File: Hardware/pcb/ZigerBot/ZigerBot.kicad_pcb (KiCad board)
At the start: 2 copper layers, 107 parts, among them J1 Motor A, J2 M Power, J3 Motor B, J4 4 Pin Male SR-04 Header, J5 USB_B_Micro, J6 3 Pin Male Servo Header, J7 3 Pin Male Servo Header, J8 3 Pin Male Servo Header, J9 3 Pin Male Servo Header, Q1 SMD-MOSFET-P-CH-20V-2A-FDN340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, SW1 SMD Button, SW2 SMD Button, SW3 SMD Button, SW4 SMD Button, U1 L7805CDT-TR, U2 DRV8833PW, U3 ATmega2560-16AU, U4 CP2102N-A01-GQFN24, Y1 16MHz Resonator

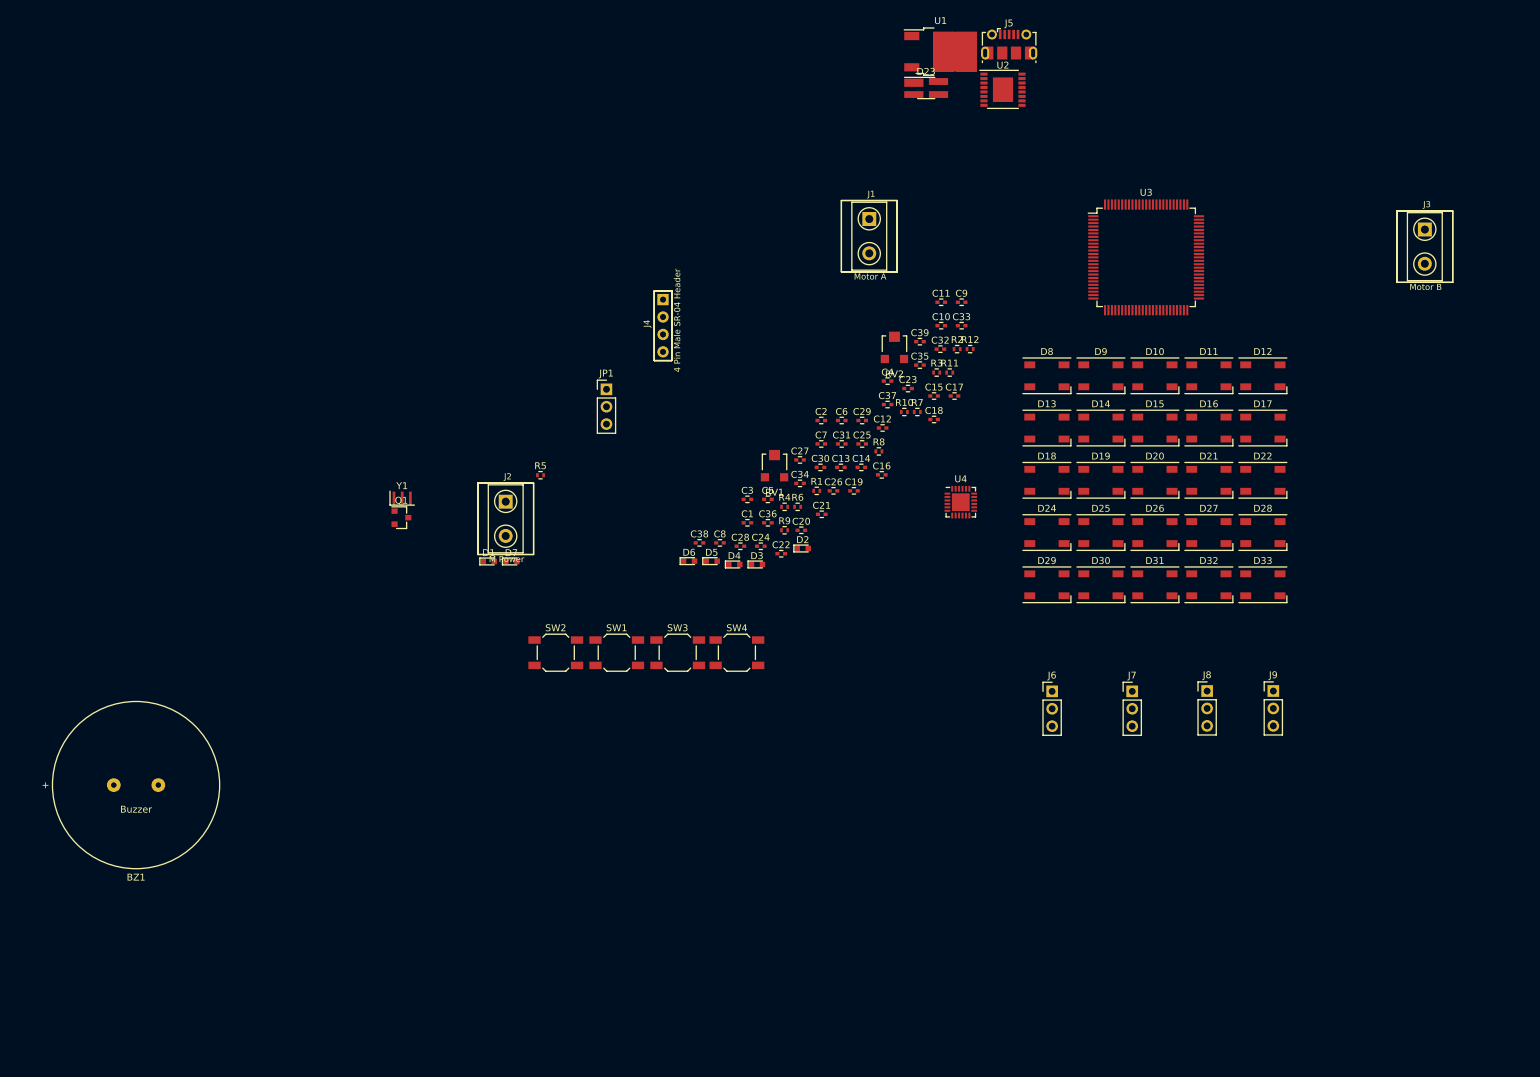
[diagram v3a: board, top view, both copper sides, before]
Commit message: LED-Matrix routed
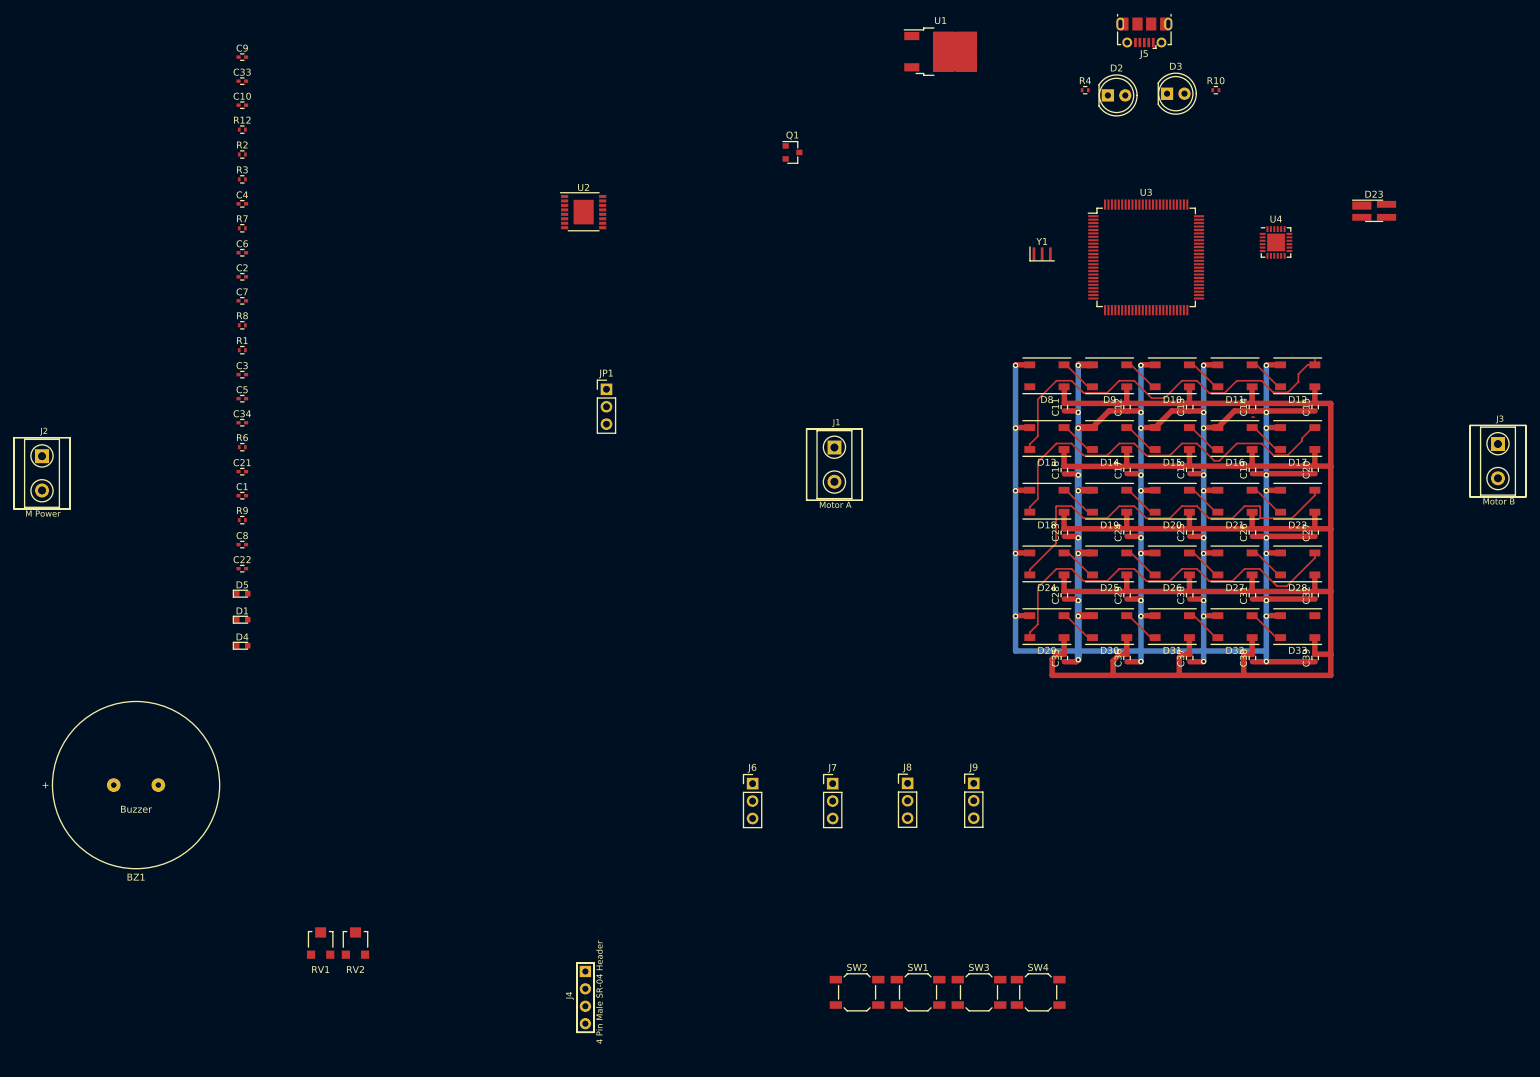
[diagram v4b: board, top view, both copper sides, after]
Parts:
- removed D6: SMD LED blue, ZigerBot:LED_0603
- removed D7: SMD LED yellow, ZigerBot:LED_0603
- removed R11, R5: 1k, Resistors_SMD:R_0402
- D2: value SMD LED blue -> LED_Dual_2pin; footprint ZigerBot:LED_0603 -> LEDs:LED_D5.0mm
- D3: value SMD LED yellow -> LED_Dual_2pin; footprint ZigerBot:LED_0603 -> LEDs:LED_D5.0mm
- moved RV2 117.2 mm to (75.7, 149.1)
- moved R12 110.9 mm to (59.2, 30.4)
- moved C9 110.8 mm to (59.2, 19.8)
- moved C33 110.8 mm to (59.2, 23.3)
- moved R2 108.0 mm to (59.2, 34.0)
- moved C10 106.9 mm to (59.2, 26.8)
- moved R3 105.1 mm to (59.2, 37.6)
- moved R7 102.0 mm to (59.2, 44.8)
- moved Y1 99.9 mm to (175.8, 48.5)
- moved J4 98.6 mm to (109.2, 157.0)
- moved C4 97.6 mm to (59.2, 41.2)
- moved RV1 96.1 mm to (70.6, 149.1)
- moved R8 94.6 mm to (59.2, 58.9)
- moved D3 91.1 mm to (194.1, 25.1)
- moved C6 90.8 mm to (59.2, 48.3)
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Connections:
- net Net-(C2-Pad2) renamed /ExtPower
- net Net-(J3-Pad1) renamed /MotOutB
- D2 pad 1: Net-(D2-Pad1) -> /MotOutA
- D3 pad 1: Net-(D3-Pad1) -> /MotInB
- D3 pad 2: Net-(D2-Pad1) -> Net-(D3-Pad2)
- J1 pad 1: Net-(D2-Pad1) -> /MotInA
- J1 pad 2: Net-(D2-Pad1) -> /MotOutA
- J3 pad 2: Net-(D6-Pad1) -> /MotInB
- R10 pad 2: Net-(D6-Pad2) -> Net-(D3-Pad2)
- R4 pad 1: Net-(R4-Pad1) -> /MotInA
- U2 pad 2: Net-(D2-Pad1) -> /MotOutA
- U2 pad 4: Net-(R4-Pad1) -> /MotInA
- U2 pad 5: Net-(D6-Pad1) -> /MotInB
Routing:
- net GND: track 0.00 -> 399.5 mm, vias 0 -> 45
- net 5V: track 0.00 -> 316.6 mm
- net Net-(D12-Pad2): track 0.00 -> 58.1 mm
- net Net-(D22-Pad2): track 0.00 -> 57.6 mm
- net Net-(D28-Pad2): track 0.00 -> 57.2 mm
- net Net-(D17-Pad2): track 0.00 -> 56.9 mm
- net Net-(D8-Pad2): track 0.00 -> 5.47 mm
- net Net-(D32-Pad2): track 0.00 -> 5.47 mm
- net Net-(D29-Pad2): track 0.00 -> 5.47 mm
- net Net-(D18-Pad2): track 0.00 -> 5.47 mm
- net Net-(D16-Pad2): track 0.00 -> 5.47 mm
- net Net-(D10-Pad4): track 0.00 -> 5.47 mm
- net Net-(D30-Pad2): track 0.00 -> 5.47 mm
- net Net-(D21-Pad2): track 0.00 -> 5.47 mm
- net Net-(D19-Pad2): track 0.00 -> 5.47 mm
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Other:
- net class Power added: clearance 0.2, trace_width 0.8, via_dia 0.8, via_drill 0.4
- net class Signal added: clearance 0.2, trace_width 0.25, via_dia 0.8, via_drill 0.4

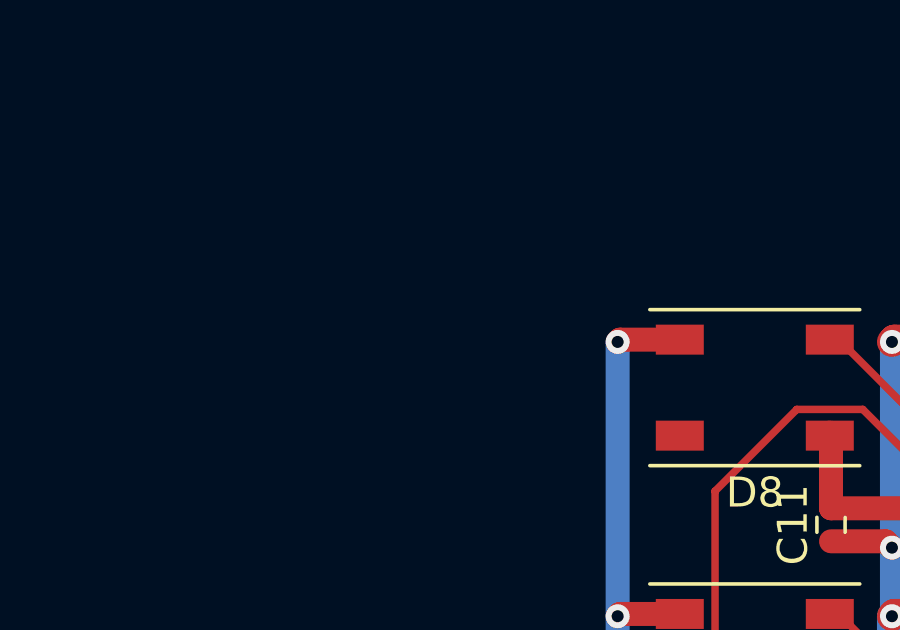
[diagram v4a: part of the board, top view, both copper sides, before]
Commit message: changed pin mappings in README
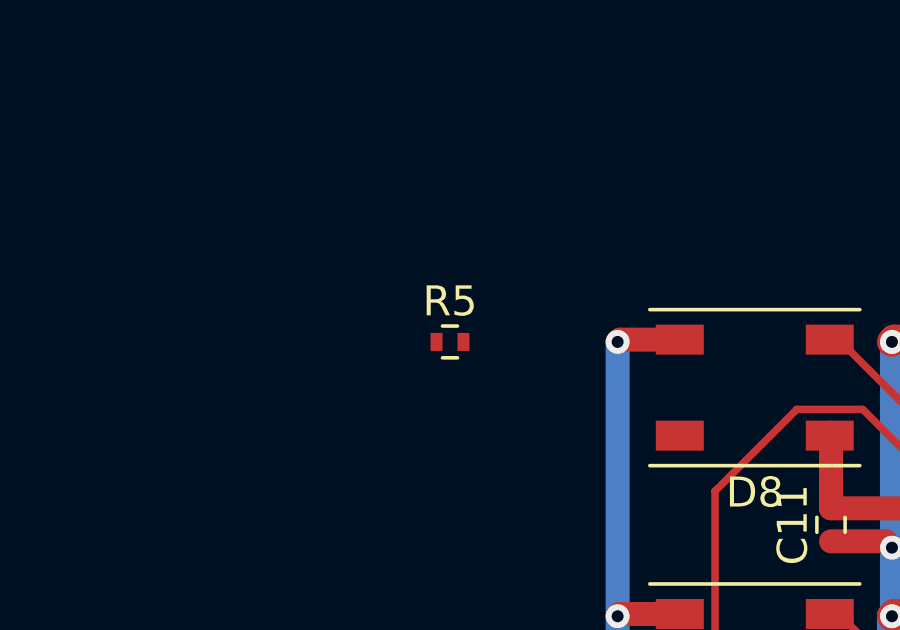
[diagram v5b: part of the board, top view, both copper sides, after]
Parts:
- added R5: 470 Ohm, Resistors_SMD:R_0402, F.Cu at (166.4, 64.8)
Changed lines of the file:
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@@
     (tracks 444)
     (zones 0)
-    (modules 103)
-    (nets 175)
+    (modules 104)
+    (nets 176)
   )
   (page A4)
@@
   (net 173 /ExtPower)
   (net 174 "Net-(D3-Pad2)")
+  (net 175 "Net-(R5-Pad1)")
   (net_class Default "This is the default net class."
     (clearance 0.2)
@@
     (add_net "Net-(R12-Pad1)")
     (add_net "Net-(R12-Pad2)")
+    (add_net "Net-(R5-Pad1)")
     (add_net "Net-(R7-Pad1)")
     (add_net "Net-(R8-Pad1)")
@@
     (add_net /TXmega)
   )
+  (module Resistors_SMD:R_0402 (layer F.Cu)
+    (at 166.37 64.77)
+    (descr "Resistor SMD 0402, reflow soldering, Vishay (see dcrcw.pdf)")
+    (tags "resistor 0402")
+    (attr smd)
+    (fp_text reference R5 (at 0 -1.35) (layer F.SilkS)
+      (effects (font (size 1 1) (thickness 0.15)))
+    )
+    (fp_text value "470 Ohm" (at 0 1.45) (layer F.Fab)
+      (effects (font (size 1 1) (thickness 0.15)))
+    )
+    (fp_line (start 0.8 0.45) (end -0.8 0.45) (layer F.CrtYd) (width 0.05))
+    (fp_line (start 0.8 0.45) (end 0.8 -0.45) (layer F.CrtYd) (width 0.05))
+    (fp_line (start -0.8 -0.45) (end -0.8 0.45) (layer F.CrtYd) (width 0.05))
+    (fp_line (start -0.8 -0.45) (end 0.8 -0.45) (layer F.CrtYd) (width 0.05))
+    (fp_line (start -0.25 0.53) (end 0.25 0.53) (layer F.SilkS) (width 0.12))
+    (fp_line (start 0.25 -0.53) (end -0.25 -0.53) (layer F.SilkS) (width 0.12))
+    (fp_line (start -0.5 -0.25) (end 0.5 -0.25) (layer F.Fab) (width 0.1))
+    (fp_line (start 0.5 -0.25) (end 0.5 0.25) (layer F.Fab) (width 0.1))
+    (fp_line (start 0.5 0.25) (end -0.5 0.25) (layer F.Fab) (width 0.1))
+    (fp_line (start -0.5 0.25) (end -0.5 -0.25) (layer F.Fab) (width 0.1))
+    (fp_text user %R (at 0 -1.35) (layer F.Fab)
+      (effects (font (size 1 1) (thickness 0.15)))
+    )
+    (pad 2 smd rect (at 0.45 0) (size 0.4 0.6) (layers F.Cu F.Paste F.Mask)
+      (net 120 "Net-(D8-Pad4)"))
+    (pad 1 smd rect (at -0.45 0) (size 0.4 0.6) (layers F.Cu F.Paste F.Mask)
+      (net 175 "Net-(R5-Pad1)"))
+    (model ${KISYS3DMOD}/Resistors_SMD.3dshapes/R_0402.wrl
+      (at (xyz 0 0 0))
+      (scale (xyz 1 1 1))
+      (rotate (xyz 0 0 0))
+    )
+  )
   (module LEDs:LED_D5.0mm (layer F.Cu)

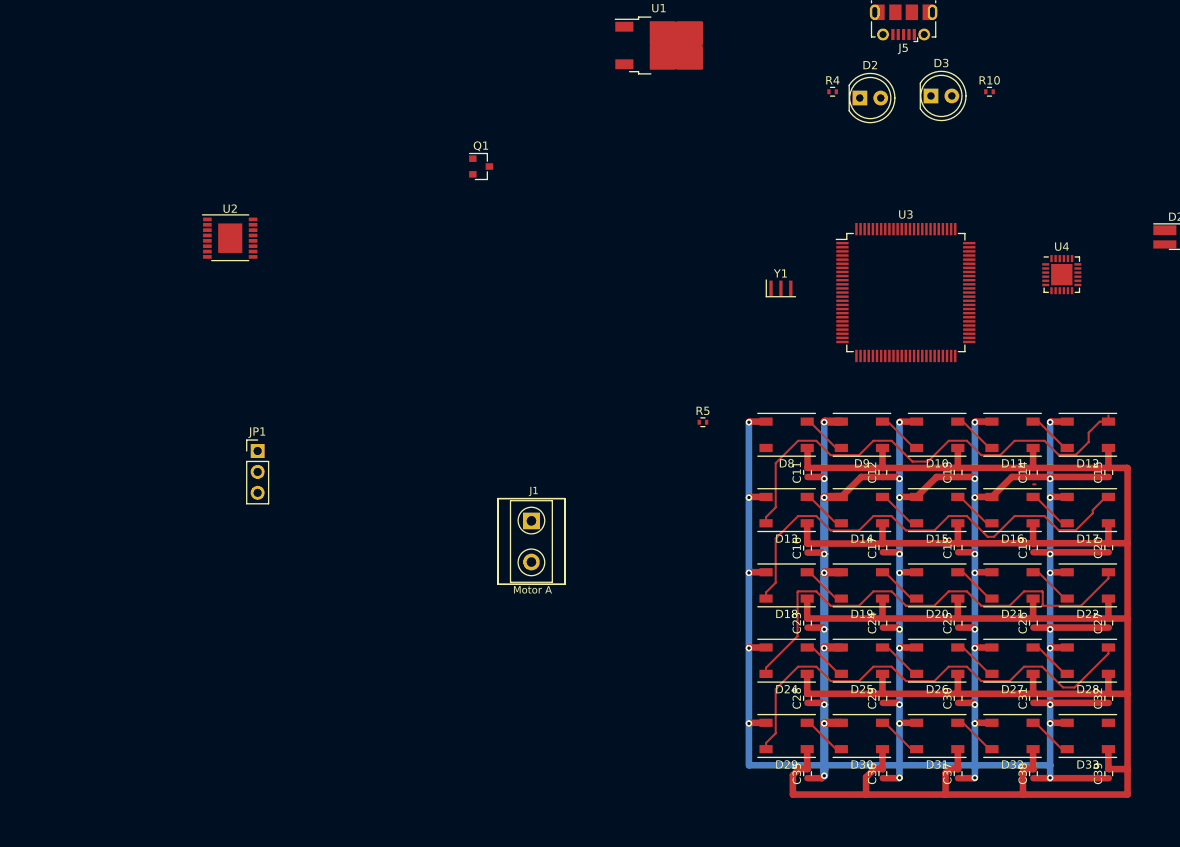
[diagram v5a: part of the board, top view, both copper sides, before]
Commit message: Added ICSP Header, Connected all peripherals to Atmega2560, updated README.md
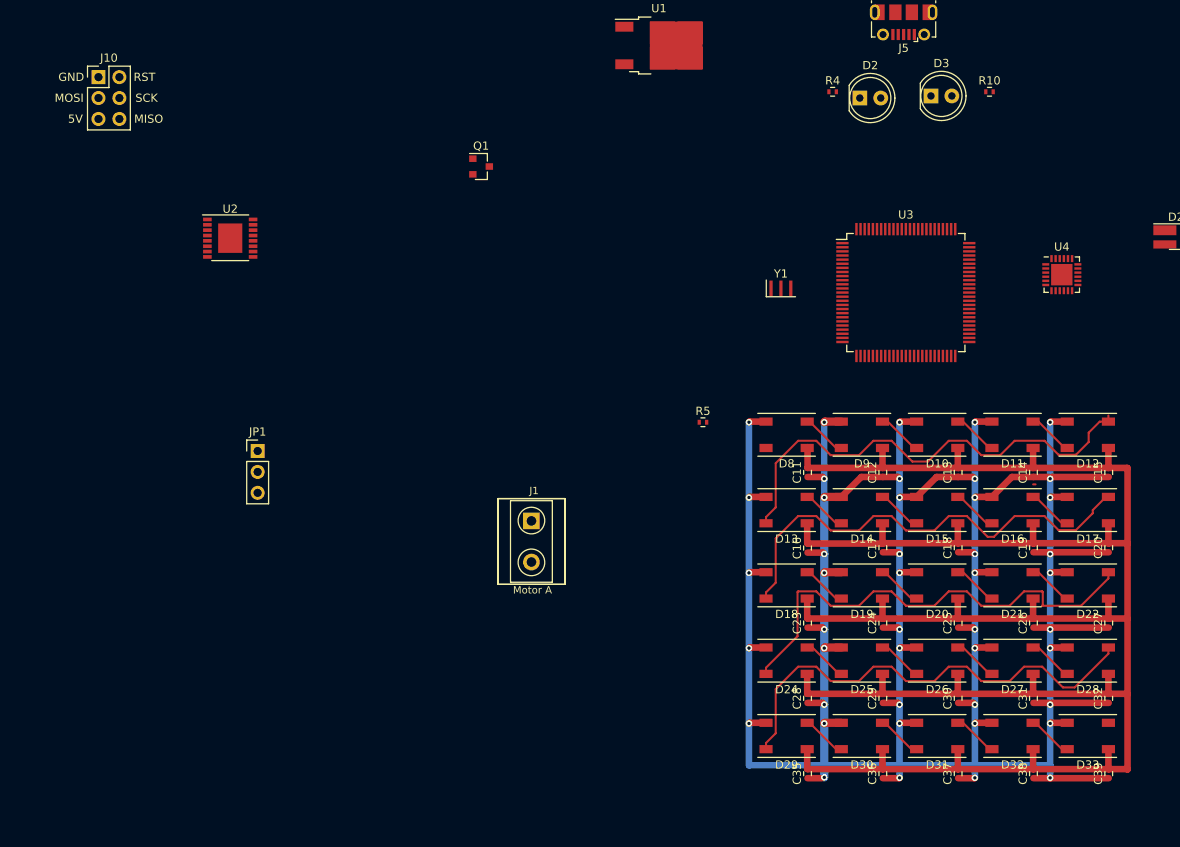
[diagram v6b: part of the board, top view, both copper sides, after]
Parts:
- added J10: ICSP, ZigerBot:ICSP, F.Cu at (93.0, 22.9)
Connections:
- net Net-(C1-Pad1) renamed /RESET
- R5 pad 1: Net-(R5-Pad1) -> /LEDMatrix
- U3 pad 15: Net-(U3-Pad15) -> /AIN2
- U3 pad 16: Net-(U3-Pad16) -> /BIN1
- U3 pad 17: Net-(U3-Pad17) -> /BIN2
- U3 pad 20: Net-(U3-Pad20) -> /SCK
- U3 pad 21: Net-(U3-Pad21) -> /MOSI
- U3 pad 22: Net-(U3-Pad22) -> /MISO
- U3 pad 5: Net-(U3-Pad5) -> /AIN1
- U3 pad 57: Net-(U3-Pad57) -> /Servo4
- U3 pad 58: Net-(U3-Pad58) -> /Servo3
- U3 pad 59: Net-(U3-Pad59) -> /Servo2
- U3 pad 60: Net-(U3-Pad60) -> /Servo1
- U3 pad 71: Net-(U3-Pad71) -> /Button4
- U3 pad 72: Net-(U3-Pad72) -> /Button3
- U3 pad 73: Net-(U3-Pad73) -> /Button2
- U3 pad 74: Net-(U3-Pad74) -> /Button1
- U3 pad 75: Net-(U3-Pad75) -> /Buzz
- U3 pad 76: Net-(U3-Pad76) -> /LEDMatrix
- U3 pad 77: Net-(U3-Pad77) -> /Echo
- U3 pad 78: Net-(U3-Pad78) -> /Trig
- U3 pad 96: Net-(U3-Pad96) -> /Pot2
- U3 pad 97: Net-(U3-Pad97) -> /Pot1
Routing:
- net 5V: track 316.6 -> 292.0 mm
